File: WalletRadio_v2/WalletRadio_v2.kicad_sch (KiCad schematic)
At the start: 43 parts, among them J1 UJC-HP-3-SMT-TR, Q1 BSP315P, Q2 Q_NPN_ECB, SW1 SW_SPDT, SW2 CUS-13TB, U1 MCP73831-2-OT, U2 Si4824, U3 LM324A

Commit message: More layout. Added fields for BOM creation.
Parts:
- removed U3: LM324A, Package_SO:SOIC-14_3.9x8.7mm_P1.27mm, symbol Amplifier_Operational:LM324A
- added FID1, FID2: Fiducial, Fiducial:Fiducial_0.75mm_Mask2.25mm, symbol Mechanical:Fiducial
- added U3: MCP6476, Package_TO_SOT_SMD:SOT-23-5_HandSoldering, symbol WalletRadio_v2:MCP6476
- BT1: Supplier (none) -> https://www.digikey.com/en/products/detail/adafruit-industr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
- D1: Supplier (none) -> https://www.digikey.com/en/products/detail/dialight/5988070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
- D2: Supplier (none) -> https://www.digikey.com/en/products/detail/bourns-inc/5-0SM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
- D3: renamed from D4; Supplier (none) -> https://www.digikey.com/en/products/detail/rohm-semiconduct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
- D4: renamed from D3; Supplier (none) -> https://www.digikey.com/en/products/detail/dialight/5988030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
- J1: Supplier (none) -> https://www.digikey.com/en/products/detail/cui-devices/ujc-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
- LS1: Supplier (none) -> https://www.digikey.com/products/en?keywords=SP-1511S-1
- Q1: Supplier (none) -> https://www.mouser.com/ProductDetail/Infineon-Technologies/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
- Q2: Supplier (none) -> https://www.digikey.com/en/products/detail/nexperia-usa-inc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
- R6: renamed from R8; Supplier (none) -> https://www.digikey.com/en/products/detail/bourns-inc/3352T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
- S1, S2: Supplier (none) -> https://www.digikey.com/en/products/detail/cui-devices/TS05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
- SW1: Supplier (none) -> https://www.digikey.com/en/products/detail/nidec-copal-elec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
- U1: Supplier (none) -> https://www.mouser.com/ProductDetail/Microchip-Technology/M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
- U2: Supplier (none) -> https://www.arrow.com/en/products/si4824-a10-cur/skyworks-s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
- renumbered R12 to R10, R13 to R11, R14 to R12, R15 to R13, R3 to R2, R4 to R3, R5 to R4, R7 to R5, R9 to R7, R10 to R8, R11 to R9
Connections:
- net +Vbat: now also U3.5 (Vdd)
- net GND: now also U3.2 (Vss)
- net at C6.1, U2.24 (AOUT): now also U3.3 (+)
- net at C7.2, Q2.1 (E): now also U3.4 (-)
- net at Q2.3 (B), TP3.1: now also U3.1 (Vout)
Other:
- moved on the sheet: TP3

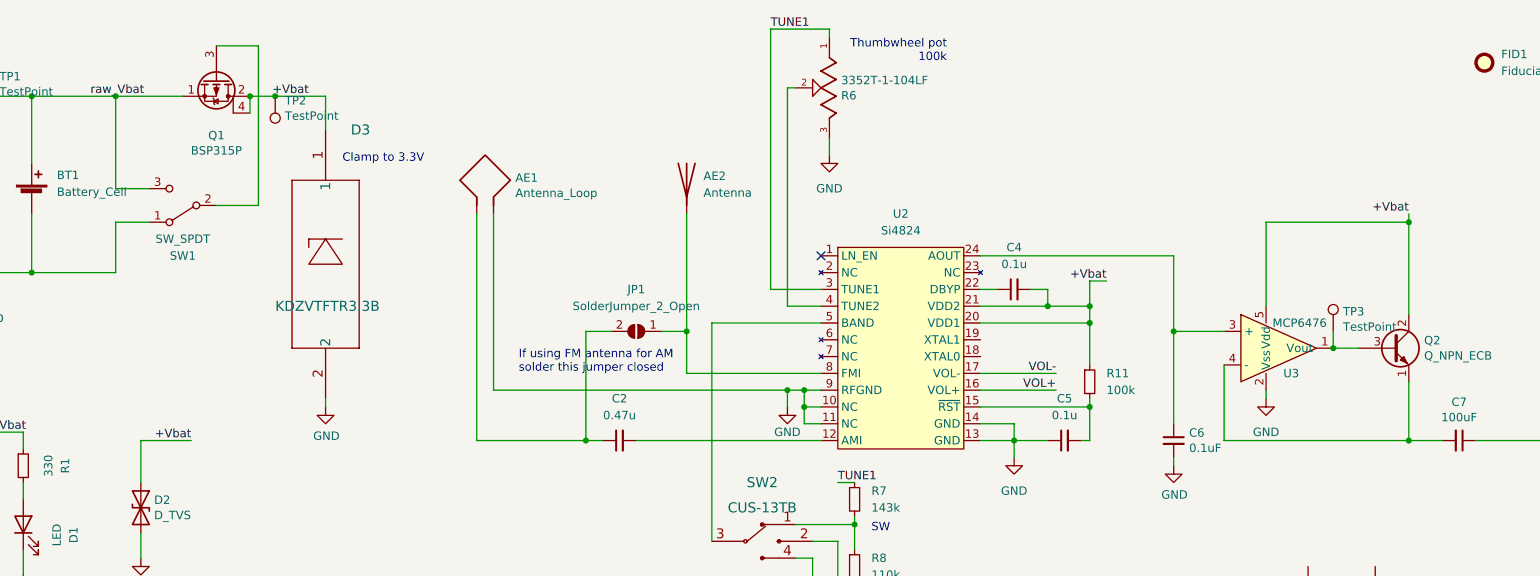
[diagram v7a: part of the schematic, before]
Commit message: Had to change some components because they were out of stock
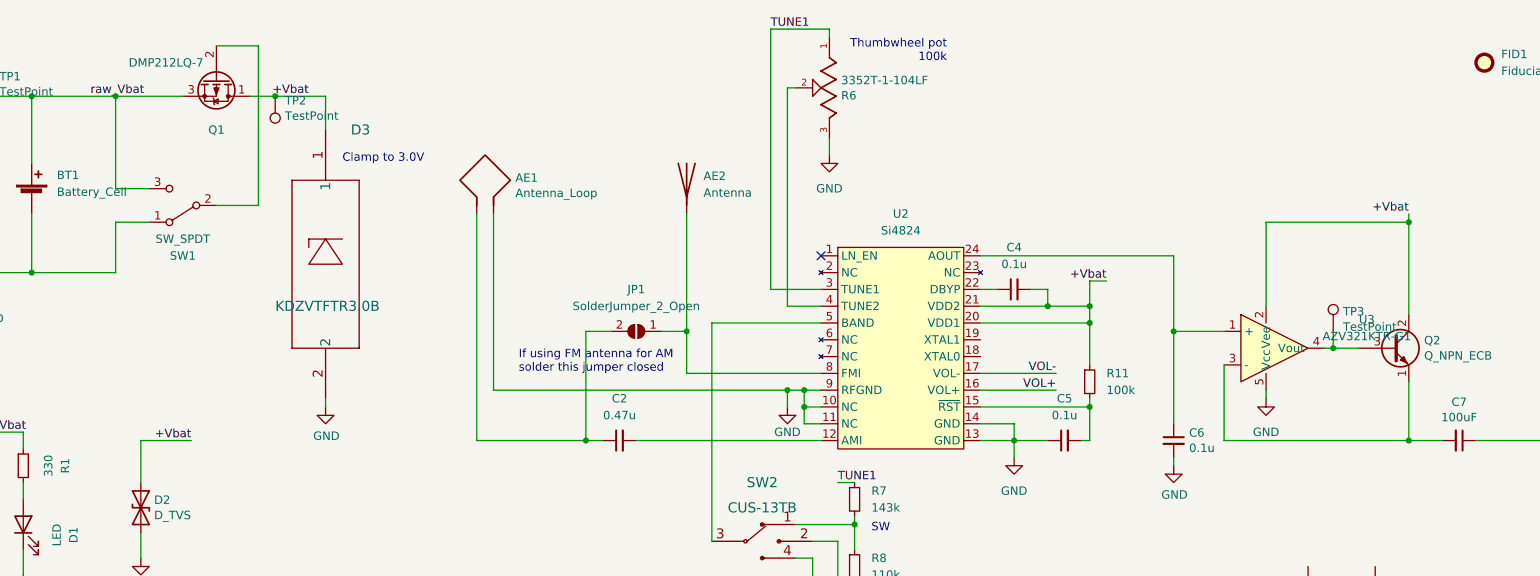
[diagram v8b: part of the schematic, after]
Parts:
- removed Q1: BSP315P, Package_TO_SOT_SMD:SOT-223, symbol Device:Q_PMOS_SDGD
- removed U3: MCP6476, Package_TO_SOT_SMD:SOT-23-5_HandSoldering, symbol WalletRadio_v2:MCP6476
- added Q1: DMP212LQ-7, Package_TO_SOT_SMD:SOT-23_Handsoldering, symbol Device:Q_PMOS_DGS
- added U3: AZV321KTR-G1, Package_TO_SOT_SMD:SOT-23-5, symbol WalletRadio_v2:AZV321KTR-G1
- C6: value 0.1uF -> 0.1u
- D3: value KDZVTFTR3.3B -> KDZVTFTR3.0B; Supplier https://www.digikey.com/en/products/detail/rohm-semiconductor/KDZVTFTR3-3B/9697261?s=N4IgTCBcDaINIBEBaA1AKgMTQJQMwDpcAhEAXQF8g -> https://www.digikey.com/en/products/detail/rohm-semiconductor/kdzvtftr3-0b/9697260
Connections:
- net +Vbat: now also Q1.1 (D), U3.2 (Vee)
- net GND: now also U3.5 (Vcc)
- net raw_Vbat: now also Q1.3 (S)
- net at C7.2, Q2.1 (E): now also U3.3 (-)
- net at Q2.3 (B), TP3.1: now also U3.4 (Vout)
- net at C6.1, U2.24 (AOUT): now also U3.1 (+)
- net at SW1.2 (B): now also Q1.2 (G)
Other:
- note added: "Clamp to 3.0V"
- note removed: "Clamp to 3.3V"
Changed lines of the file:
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@@
   (junction (at 139.7 158.75) (diameter 0) (color 0 0 0 0)
   )
-  (junction (at 60.96 27.94) (diameter 0) (color 0 0 0 0)
-  )
   (junction (at 237.49 137.16) (diameter 0) (color 0 0 0 0)
   )
   (junction (at 142.24 72.39) (diameter 0) (color 0 0 0 0)
   )
+  (junction (at 187.96 74.93) (diameter 0) (color 0 0 0 0)
+  )
   (junction (at 224.79 66.04) (diameter 0) (color 0 0 0 0)
-  )
-  (junction (at 187.96 74.93) (diameter 0) (color 0 0 0 0)
   )
   (junction (at 40.64 27.94) (diameter 0) (color 0 0 0 0)
@@
     (stroke (width 0) (type default) (color 0 0 0 0))
   )
+  (wire (pts (xy 223.52 66.04) (xy 224.79 66.04))
+    (stroke (width 0) (type default) (color 0 0 0 0))
+  )
   (wire (pts (xy 246.38 80.01) (xy 259.08 80.01))
     (stroke (width 0) (type default) (color 0 0 0 0))
@@
   )
   (wire (pts (xy 130.81 146.05) (xy 139.7 146.05))
-    (stroke (width 0) (type default) (color 0 0 0 0))
-  )
-  (wire (pts (xy 60.96 30.48) (xy 60.96 27.94))
     (stroke (width 0) (type default) (color 0 0 0 0))
   )
@@
     (effects (font (size 1.27 1.27)) (justify left bottom))
   )
-  (text "Clamp to 3.3V" (at 74.93 38.1 0)
+  (text "Clamp to 3.0V" (at 74.93 38.1 0)
     (effects (font (size 1.27 1.27)) (justify left bottom))
   )
@@
       (effects (font (size 1.27 1.27)) (justify left))
     )
-    (property "Value" "0.1uF" (id 1) (at 202.9968 81.153 0)
+    (property "Value" "0.1u" (id 1) (at 202.9968 81.153 0)
       (effects (font (size 1.27 1.27)) (justify left))
     )
@@
     )
     (pin "1")
-  )
-  (symbol (lib_id "Device:Q_PMOS_SDGD") (at 55.88 25.4 270) (unit 1)
-    (in_bom yes) (on_board yes)
-    (property "Reference" "Q1" (id 0) (at 55.88 33.8582 90))
-    (property "Value" "BSP315P" (id 1) (at 55.88 36.1696 90))
-    (property "Footprint" "Package_TO_SOT_SMD:SOT-223" (id 2) (at 58.42 30.48 0)
-      (effects (font (size 1.27 1.27)) hide)
-    )
-    (property "Datasheet" "https://www.infineon.com/dgdl/Infineon-BSP315P-DS-v01_07-en.pdf?fileId=db3a30433b47825b013b6015cc1558b9" (id 3) (at 55.88 25.4 0)
-      (effects (font (size 1.27 1.27)) hide)
-    )
-    (property "Supplier" "https://www.mouser.com/ProductDetail/Infineon-Technologies/BSP315PH6327XTSA1?qs=LqwxS8kK3AuIaykNQn76SA%3D%3D" (id 4) (at 55.88 25.4 90)
-      (effects (font (size 1.27 1.27)) hide)
-    )
-    (pin "1")
-    (pin "2")
-    (pin "3")
-    (pin "4")
   )
   (symbol (lib_id "3352T-1-103LF:3352T-1-103LF") (at 148.59 26.67 270) (unit 1)
@@
       (effects (font (size 1.524 1.524)) (justify left))
     )
-    (property "Value" "KDZVTFTR3.3B" (id 1) (at 64.77 59.69 90)
+    (property "Value" "KDZVTFTR3.0B" (id 1) (at 64.77 59.69 90)
       (effects (font (size 1.524 1.524)) (justify left))
     )
@@
       (effects (font (size 1.524 1.524)) hide)
     )
-    (property "Supplier" "https://www.digikey.com/en/products/detail/rohm-semiconductor/KDZVTFTR3-3B/9697261?s=N4IgTCBcDaINIBEBaA1AKgMTQJQMwDpcAhEAXQF8g" (id 4) (at 72.39 33.02 90)
+    (property "Supplier" "https://www.digikey.com/en/products/detail/rohm-semiconductor/kdzvtftr3-0b/9697260" (id 4) (at 72.39 33.02 90)
       (effects (font (size 1.27 1.27)) hide)
     )
@@
     (pin "2")
   )
-  (symbol (lib_id "WalletRadio_v2:MCP6476") (at 215.9 66.04 0) (unit 1)
-    (in_bom yes) (on_board yes)
-    (property "Reference" "U3" (id 0) (at 218.44 69.85 0))
-    (property "Value" "MCP6476" (id 1) (at 219.71 62.23 0))
-    (property "Footprint" "Package_TO_SOT_SMD:SOT-23-5_HandSoldering" (id 2) (at 215.9 74.93 0)
-      (effects (font (size 1.27 1.27)) hide)
-    )
-    (property "Datasheet" "https://ww1.microchip.com/downloads/en/DeviceDoc/MCP6476-6R-6U-7-9-Data-Sheet-20006419B.pdf" (id 3) (at 215.9 74.93 0)
-      (effects (font (size 1.27 1.27)) hide)
-    )
-    (property "Supplier" "https://www.digikey.com/en/products/detail/microchip-technology/MCP6476UT-E-LT/13986071" (id 4) (at 215.9 66.04 0)
+  (symbol (lib_id "Device:Q_PMOS_DGS") (at 55.88 25.4 270) (unit 1)
+    (in_bom yes) (on_board yes)
+    (property "Reference" "Q1" (id 0) (at 55.88 33.02 90))
+    (property "Value" "DMP212LQ-7" (id 1) (at 48.26 22.86 90))
+    (property "Footprint" "Package_TO_SOT_SMD:SOT-23_Handsoldering" (id 2) (at 58.42 30.48 0)
+      (effects (font (size 1.27 1.27)) hide)
+    )
+    (property "Datasheet" "https://www.diodes.com/assets/Datasheets/DMP2123LQ.pdf" (id 3) (at 55.88 25.4 0)
+      (effects (font (size 1.27 1.27)) hide)
+    )
+    (property "Supplier" "https://www.digikey.com/en/products/detail/diodes-incorporated/DMP2123LQ-7/5768836" (id 4) (at 55.88 25.4 90)
       (effects (font (size 1.27 1.27)) hide)
     )
@@
     (pin "2")
     (pin "3")
-    (pin "4")
-    (pin "5")
   )
   (symbol (lib_id "power:GND") (at 91.44 171.45 0) (unit 1)
@@
     )
     (pin "1")
+  )
+  (symbol (lib_id "WalletRadio_v2:AZV321KTR-G1") (at 214.63 66.04 0) (unit 1)
+    (in_bom yes) (on_board yes) (fields_autoplaced)
+    (property "Reference" "U3" (id 0) (at 229.87 61.7093 0))
+    (property "Value" "AZV321KTR-G1" (id 1) (at 229.87 64.2493 0))
+    (property "Footprint" "Package_TO_SOT_SMD:SOT-23-5" (id 2) (at 214.63 66.04 0)
+      (effects (font (size 1.27 1.27)) hide)
+    )
+    (property "Datasheet" "https://www.diodes.com/assets/Datasheets/AZV321.pdf" (id 3) (at 214.63 66.04 0)
+      (effects (font (size 1.27 1.27)) hide)
+    )
+    (property "Supplier" "https://www.digikey.com/en/products/detail/diodes-incorporated/AZV321KTR-G1/4471050" (id 4) (at 214.63 66.04 0)
+      (effects (font (size 1.27 1.27)) hide)
+    )
+    (pin "1")
+    (pin "2")
+    (pin "3")
+    (pin "4")
+    (pin "5")
   )
   (symbol (lib_id "WalletRadio_v2:TS05-66-43-BK-260-SMT-67") (at 226.06 149.86 90) (unit 1)
@@
     )
     (path "/00000000-0000-0000-0000-00005eff08d4"
-      (reference "C6") (unit 1) (value "0.1uF") (footprint "Capacitor_SMD:C_0603_1608Metric_Pad1.08x0.95mm_HandSolder")
+      (reference "C6") (unit 1) (value "0.1u") (footprint "Capacitor_SMD:C_0603_1608Metric_Pad1.08x0.95mm_HandSolder")
     )
     (path "/00000000-0000-0000-0000-00005ef93ce9"
@@
     )
     (path "/13498cf5-6c74-4e9c-b682-1adf90fce80e"
-      (reference "D3") (unit 1) (value "KDZVTFTR3.3B") (footprint "WalletRadio:KDZVTFTR3.3B")
+      (reference "D3") (unit 1) (value "KDZVTFTR3.0B") (footprint "WalletRadio:KDZVTFTR3.3B")
     )
     (path "/d01b05b9-a01c-44e0-93fd-3ec93d9dff2b"
@@
       (reference "LS1") (unit 1) (value "8 Ohm Speaker") (footprint "WalletRadio:Wall")
     )
-    (path "/00000000-0000-0000-0000-000061fcc399"
-      (reference "Q1") (unit 1) (value "BSP315P") (footprint "Package_TO_SOT_SMD:SOT-223")
+    (path "/378f207e-d5d6-444a-9507-357bf3b55e8f"
+      (reference "Q1") (unit 1) (value "DMP212LQ-7") (footprint "Package_TO_SOT_SMD:SOT-23_Handsoldering")
     )
     (path "/00000000-0000-0000-0000-00005efb3d6e"
@@
       (reference "U2") (unit 1) (value "Si4824") (footprint "Package_SO:SSOP-24_3.9x8.7mm_P0.635mm")
     )
-    (path "/33476ae4-279a-420f-aadf-3d16395404ed"
-      (reference "U3") (unit 1) (value "MCP6476") (footprint "Package_TO_SOT_SMD:SOT-23-5_HandSoldering")
-    )
-  )
+    (path "/c7dd7881-1d83-408c-ae42-4609552325e9"
+      (reference "U3") (unit 1) (value "AZV321KTR-G1") (footprint "Package_TO_SOT_SMD:SOT-23-5")
+    )
+  )
